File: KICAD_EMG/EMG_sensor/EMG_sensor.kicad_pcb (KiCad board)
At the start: 2 copper layers, 41 x 34 mm, 42 parts, among them J1 Conn_01x03_Pin, J2 Conn_01x01_Pin, J3 Conn_01x01_Pin, J4 Conn_01x01_Pin, J5 Conn_01x02_Pin, U1 TL081, U2 TL081, U3 TL081, U4 TL081, U5 TL081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

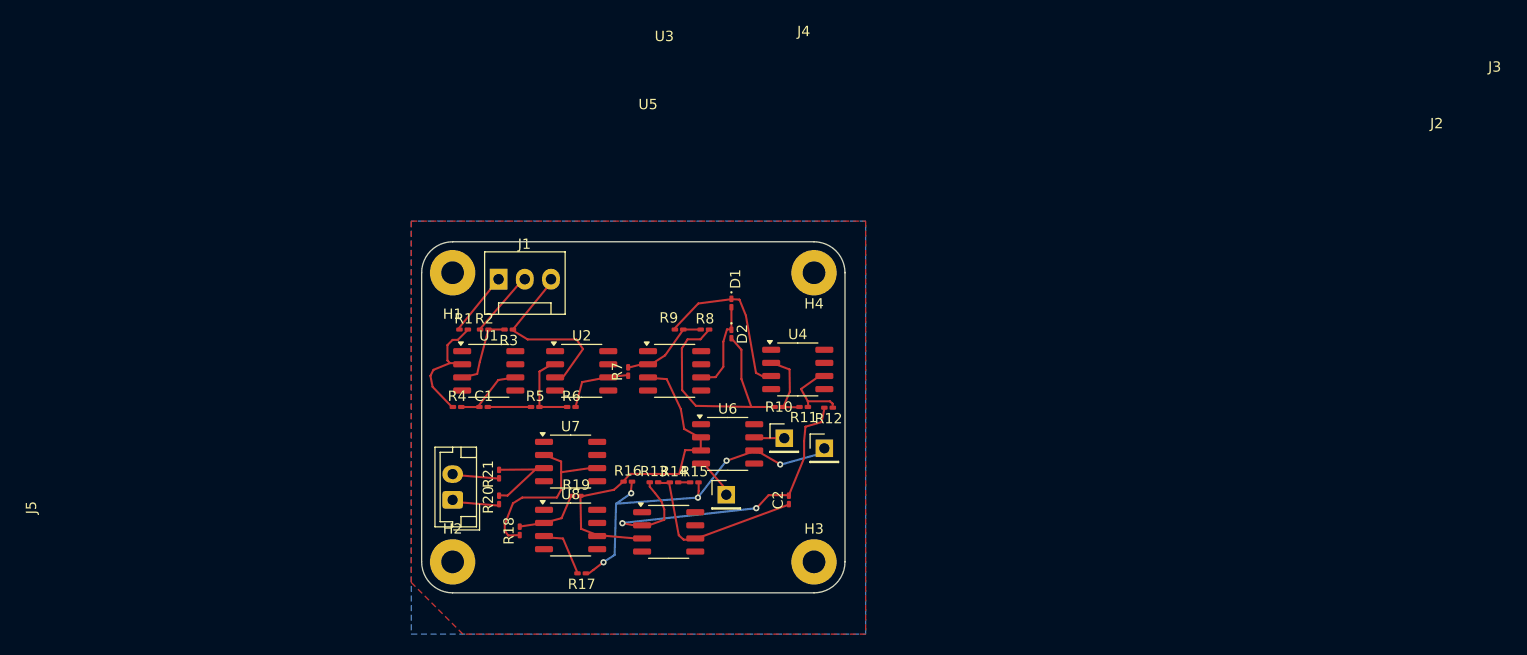
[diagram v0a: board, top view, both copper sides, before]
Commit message: le PCB avec les piste à 0.3 et 0 erreur
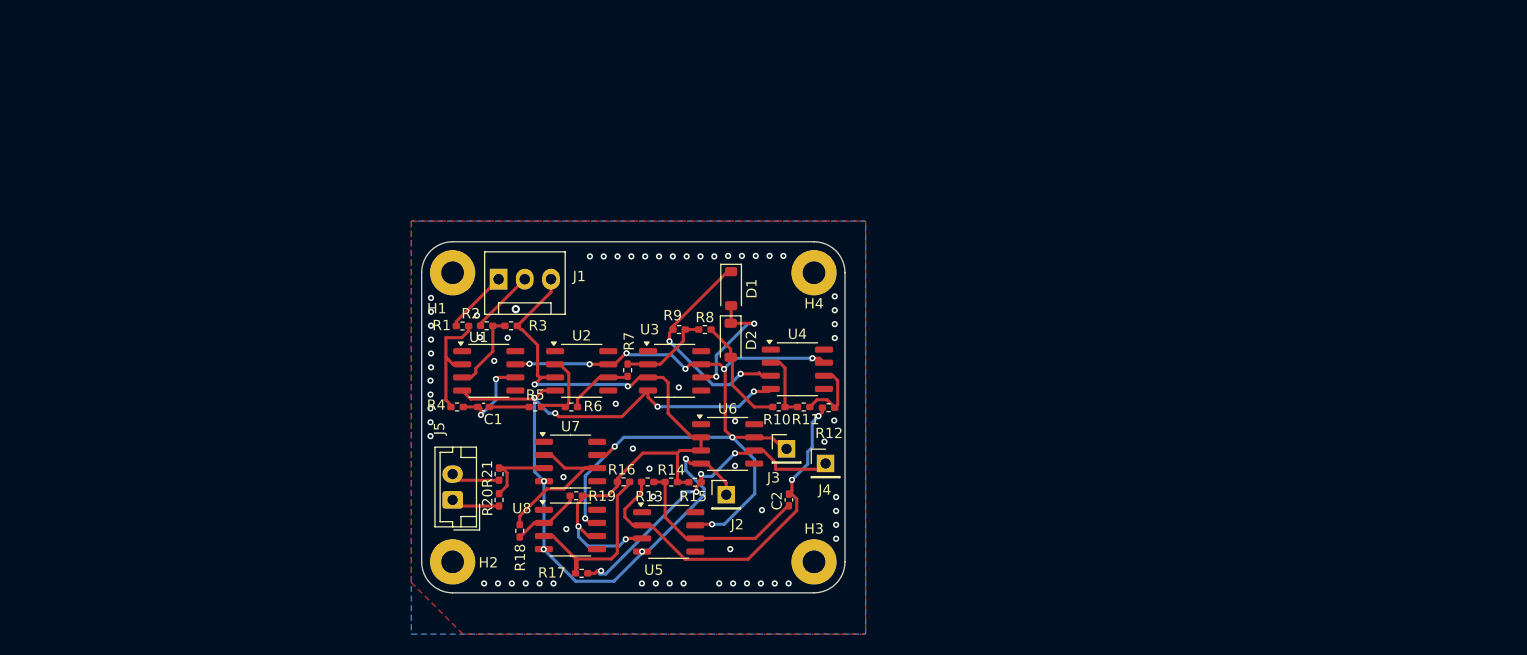
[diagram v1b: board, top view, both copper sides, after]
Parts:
- C1, C2: footprint Capacitor_SMD:C_0201_0603Metric_Pad0.64x0.40mm_HandSolder -> Capacitor_SMD:C_0402_1005Metric_Pad0.74x0.62mm_HandSolder
- D1, D2: footprint Diode_SMD:D_0201_0603Metric_Pad0.64x0.40mm_HandSolder -> Diode_SMD:D_SOD-123
- R1, R10, R11, R12, R13, R14, R15, R16, R17, R18, R19, R2, R20, R21, R3, R4, R5, R6, R7, R8, R9: footprint Resistor_SMD:R_0201_0603Metric_Pad0.64x0.40mm_HandSolder -> Resistor_SMD:R_0402_1005Metric_Pad0.72x0.64mm_HandSolder
- moved J4 1.47 mm to (152.1, 96.5)
- moved D1 1.39 mm to (143.0, 79.5)
- moved J3 1.06 mm to (148.3, 95.1)
- moved D2 0.61 mm to (142.9, 84.5)
- moved R13 0.61 mm to (134.9, 98.3)
- moved R2 0.43 mm to (119.3, 83.1)
- moved R3 0.43 mm to (121.7, 83.1)
- moved R16 0.41 mm to (132.6, 98.2)
- moved R1 0.36 mm to (117.0, 83.2)
- moved R14 0.27 mm to (137.2, 98.3)
- moved R7 0.14 mm to (132.9, 87.4)
- moved R15 0.07 mm to (139.5, 98.3)
- turned R18 to -90 degrees
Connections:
- U1 pad 4: -15V -> Net-(J2-Pin_1)
- U1 pad 7: +15V -> Net-(J3-Pin_1)
- U2 pad 4: -15V -> Net-(J2-Pin_1)
- U2 pad 7: +15V -> Net-(J3-Pin_1)
- U3 pad 4: -15V -> Net-(J2-Pin_1)
- U3 pad 7: +15V -> Net-(J3-Pin_1)
- U4 pad 4: -15V -> Net-(J2-Pin_1)
- U4 pad 7: +15V -> Net-(J3-Pin_1)
- U5 pad 4: -15V -> Net-(J2-Pin_1)
- U5 pad 7: +15V -> Net-(J3-Pin_1)
- U7 pad 4: -15V -> Net-(J2-Pin_1)
- U7 pad 7: +15V -> Net-(J3-Pin_1)
- U8 pad 4: -15V -> Net-(J2-Pin_1)
- U8 pad 7: +15V -> Net-(J3-Pin_1)
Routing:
- net Net-(J2-Pin_1): track 0.00 -> 82.3 mm, vias 0 -> 8
- net Net-(J3-Pin_1): track 0.00 -> 81.1 mm, vias 0 -> 10
- net Net-(J1-Pin_3): track 0.00 -> 68.9 mm, vias 0 -> 4
- net Net-(U5--): track 0.00 -> 36.2 mm
- net Net-(J4-Pin_1): track 0.00 -> 31.5 mm, vias 5 -> 4
- net Net-(D1-K): track 0.00 -> 21.7 mm, vias 0 -> 2
- net Net-(C2-Pad1): track 0.00 -> 18.8 mm
- net Net-(U8-+): track 0.00 -> 18.0 mm
- net Net-(U7--): track 0.00 -> 15.9 mm
- net Net-(D1-A): track 0.00 -> 12.5 mm, vias 0 -> 2
- net Net-(U1--): track 0.00 -> 11.8 mm
- net Net-(D2-A): track 0.00 -> 11.2 mm
- net Net-(U3--): track 0.00 -> 9.14 mm
- net Net-(C1-Pad1): track 0.00 -> 8.60 mm, vias 0 -> 2
- net Net-(U1-+): track 0.00 -> 8.29 mm
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
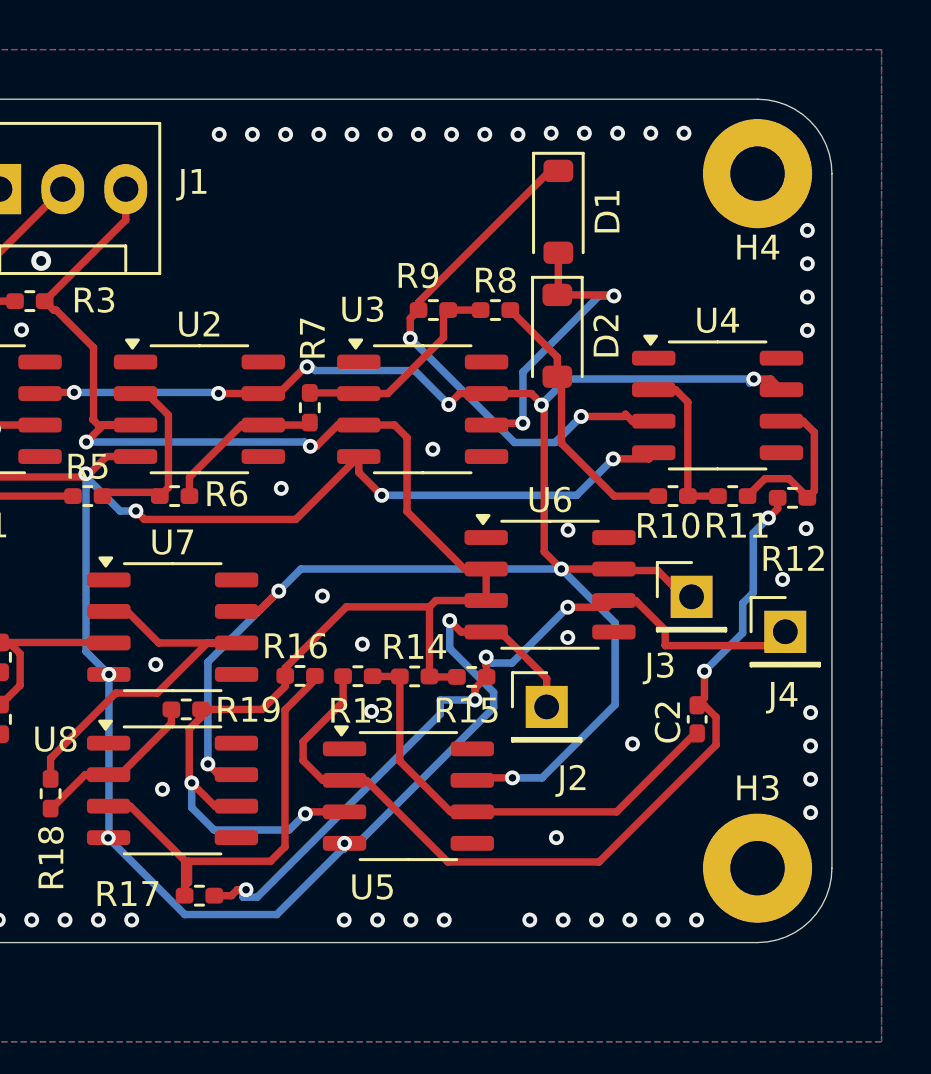
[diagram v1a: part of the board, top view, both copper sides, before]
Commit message: PCB modifié et envoyé en ticket
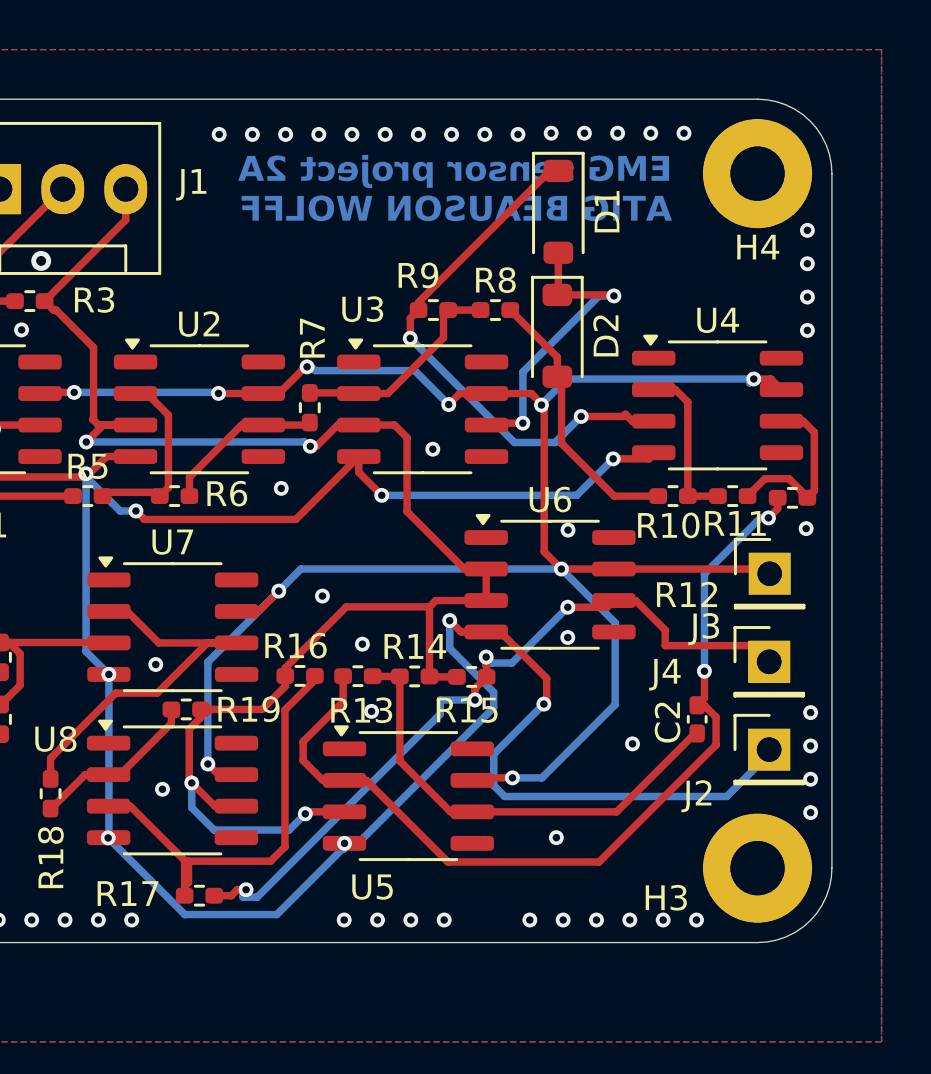
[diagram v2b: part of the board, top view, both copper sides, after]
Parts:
- moved J2 9.13 mm to (151.5, 101.2)
- moved J3 3.28 mm to (151.5, 94.1)
- moved J4 1.37 mm to (151.5, 97.7)
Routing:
- net Net-(J2-Pin_1): track 82.3 -> 98.4 mm, vias 8 -> 9
- net Net-(J3-Pin_1): track 81.1 -> 84.0 mm
- net Net-(J4-Pin_1): track 31.5 -> 30.9 mm
- net GND: vias 68 -> 67
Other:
- board text added: "EMG sensor project 2A ATIG BEAUSON WOLFF"
